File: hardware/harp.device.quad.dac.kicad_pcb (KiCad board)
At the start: 4 copper layers, 90 x 100 mm, 286 parts, among them J1 5-146281-3, J10 Conn_Coaxial, J11 Conn_Coaxial, J12 Conn_Coaxial, J13 Conn_Coaxial, J14 Barrel_Jack_Switch, J15 Conn_Coaxial, J16 Conn_Coaxial, J17 Conn_Coaxial, J18 Conn_Coaxial, J2 5-146281-3, J3 AudioJack3, J4 USB_C_Receptacle_USB2.0, J5 Micro_SD_Card_Det_Hirose_DM3AT, J6 Conn_Coaxial, J7 Conn_Coaxial, J8 Conn_Coaxial, J9 Conn_Coaxial, Q1 Si2369DS, Q2 Si2369DS, Q3 Si2369DS, SW2 SPST-NO, U1 LM337_SOT223, U10 LTC2642, U11 LTC2642, U12 REF3525, U13 LMV393IDGKR, U14 LMV393IDGKR, U15 LMV393IDGKR, U16 LMV393IDGKR, U17 INA630, U18 INA630, U19 INA630, U2 W25Q16JVUXIQ, U20 INA630, U21 REF2033, U22 SN74LVC2T45DCTR, U23 SN74LVC2T45DCTR, U24 rt6150b-33gqw, U25 TPS65131RGE, U27 LM2940IMPX-12/NOPB, U29 LMR51430, U3 ADUM4160, U30 SN74LVC2T45DCTR, U31 SN74LVC2T45DCTR, U32 RP2350_80QFN, U4 OPA2994IDGKR, U5 OPA2994IDGKR, U6 OPA2994IDGKR, U7 OPA2994IDGKR, U8 LTC2642, U9 LTC2642

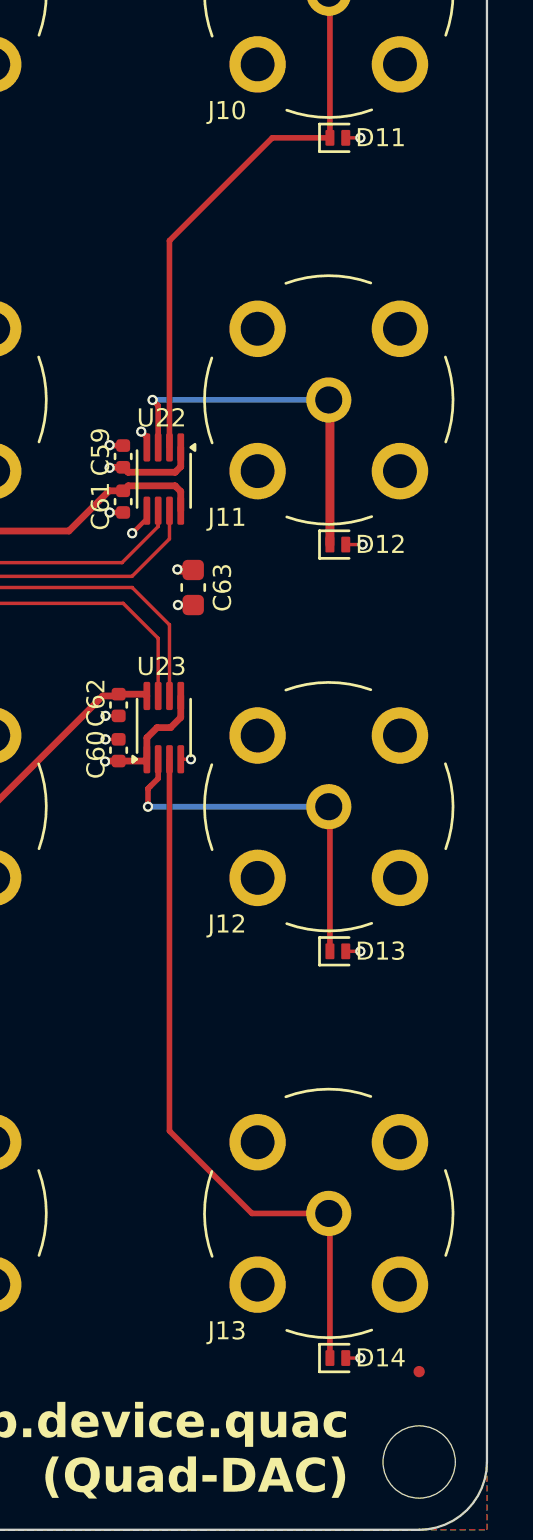
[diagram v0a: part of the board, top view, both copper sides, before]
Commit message: add pulldowns to external triggers
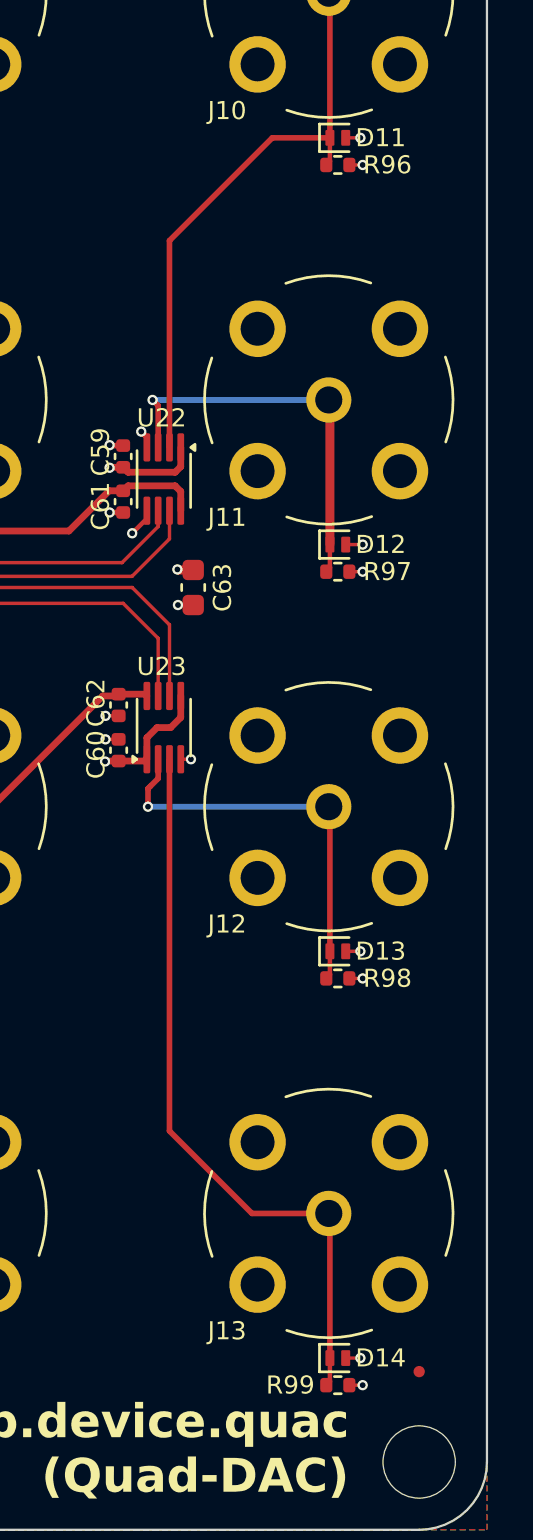
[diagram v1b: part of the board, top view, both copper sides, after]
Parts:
- added R96: 10K, Resistor_SMD:R_0402_1005Metric, F.Cu at (179.3, 69.6)
- added R97: 10K, Resistor_SMD:R_0402_1005Metric, F.Cu at (179.3, 87.6)
- added R98: 10K, Resistor_SMD:R_0402_1005Metric, F.Cu at (179.3, 105.6)
- added R99: 10K, Resistor_SMD:R_0402_1005Metric, F.Cu at (179.3, 123.6)
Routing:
- net GND: track 137.2 -> 139.6 mm, vias 178 -> 182
- net Net-(D14-A1): track 31.5 -> 32.8 mm
- net Net-(D13-A1): track 16.7 -> 18.0 mm
- net Net-(D12-A1): track 16.4 -> 17.7 mm
- net Net-(D11-A1): track 24.6 -> 25.8 mm

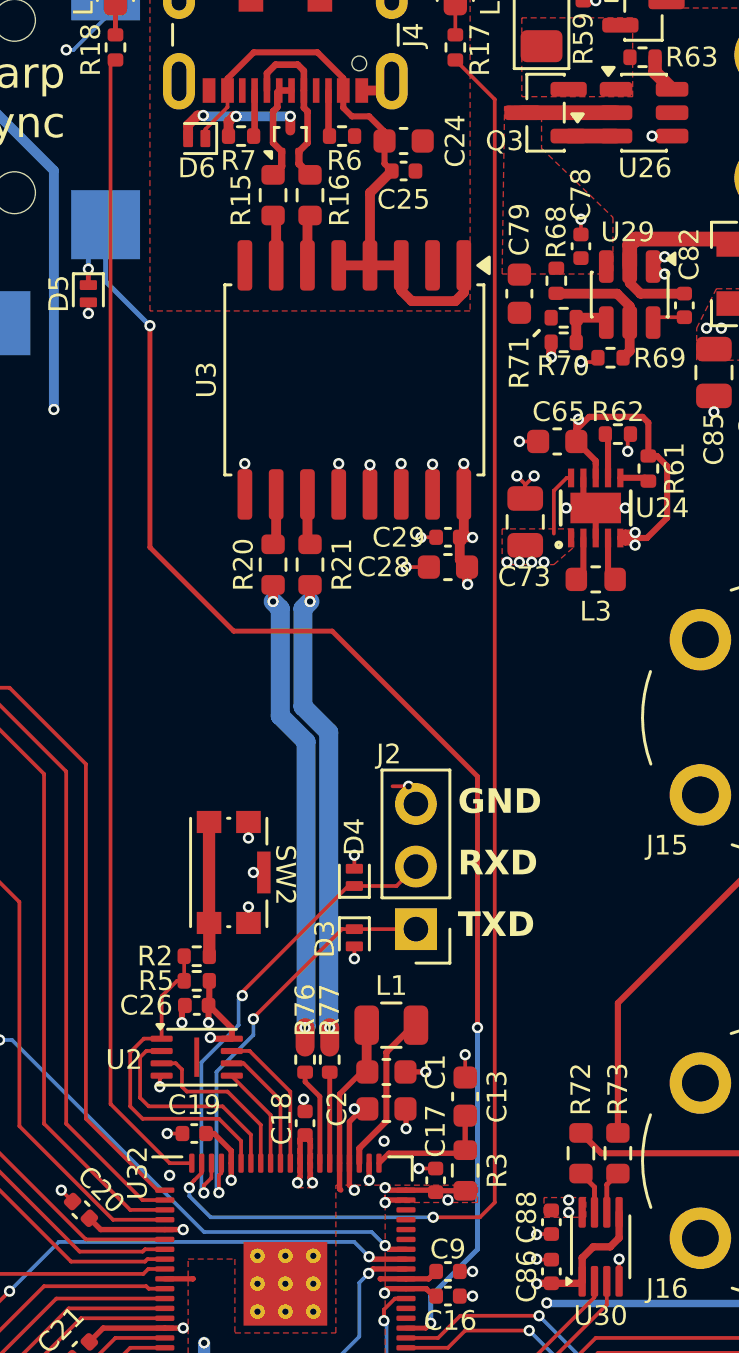
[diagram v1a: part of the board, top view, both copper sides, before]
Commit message: change R3, R15, R16, R20, R21 package to 0402
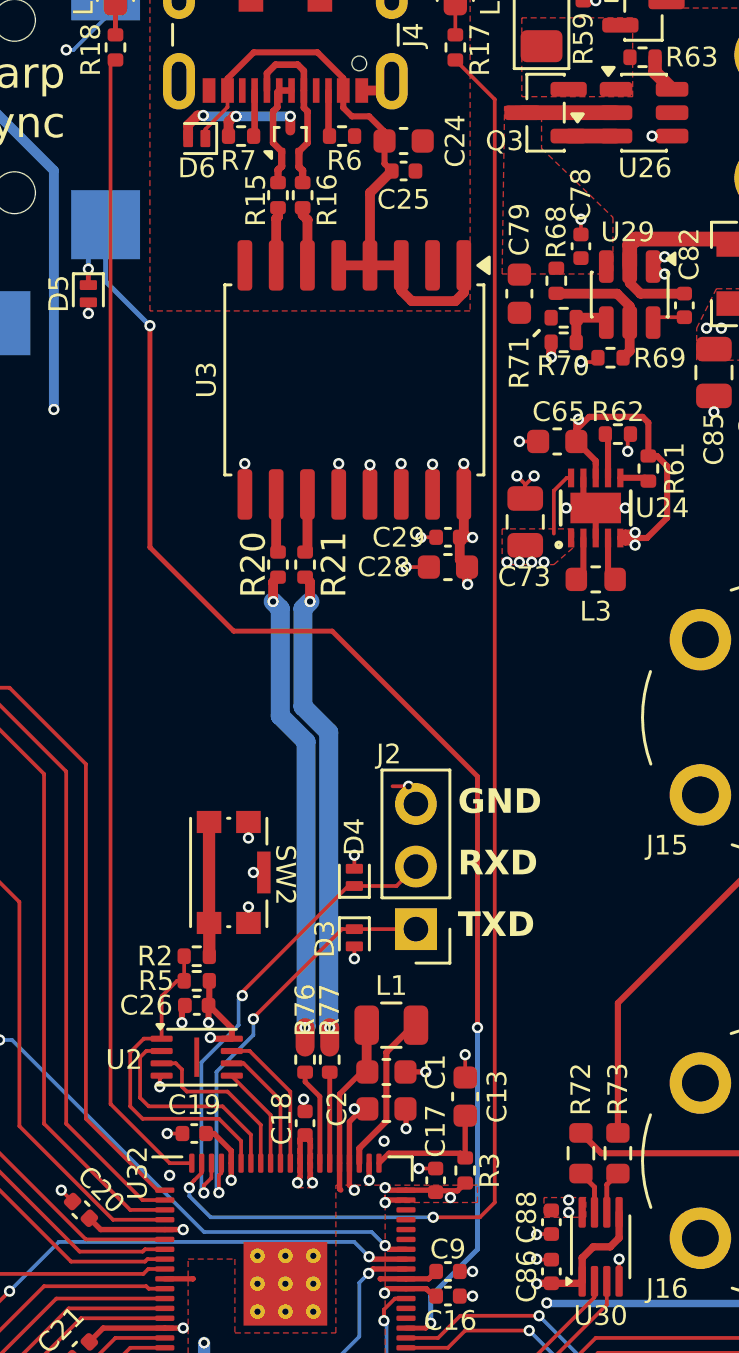
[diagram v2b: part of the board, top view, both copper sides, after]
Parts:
- R15, R16, R20, R21, R3: footprint Resistor_SMD:R_0603_1608Metric -> Resistor_SMD:R_0402_1005Metric
- moved R16 0.30 mm to (141.6, 40.8)
- moved R15 0.20 mm to (140.6, 40.8)
- moved R20 0.20 mm to (140.6, 55.8)
- moved R21 0.20 mm to (141.7, 55.8)
